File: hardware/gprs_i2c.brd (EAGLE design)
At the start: 50 x 38 mm, 88 parts, among them IC1 SIM900, J2 U.FL, Q1 si2305cd, Q2 PMBF170, Q3 PMBF170, Q4 si2305cd, Q5 si2305cd, T1 BC846, T2 BC846, T3 BC846, T4 BC846, U1 SPX5205 3v3, U3 TC1014 2V8, X2 bat, X3 prog, X4 ts, X5 MOLEX_4HORIZONTAL, X6 MOLEX_4HORIZONTAL, Y1 32768Hz CFPX-217 12.5pF

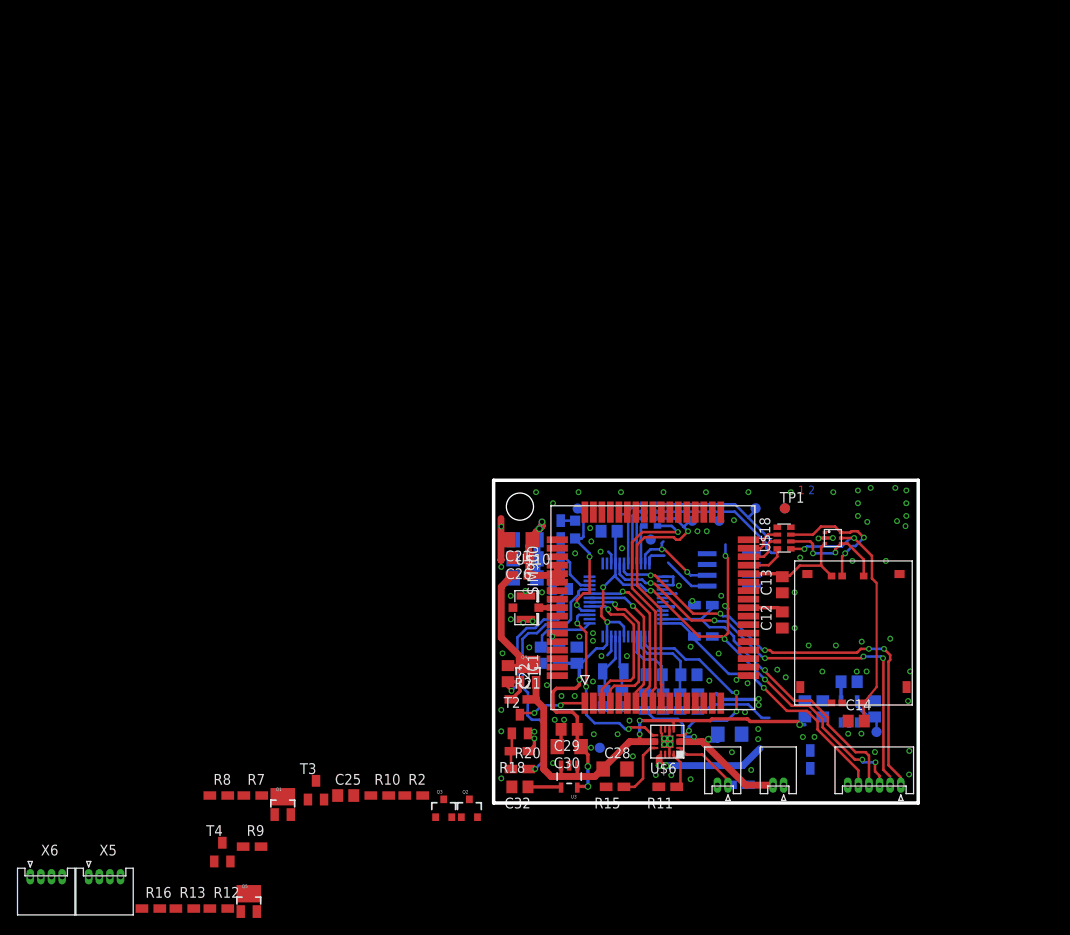
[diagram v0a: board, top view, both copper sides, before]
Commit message: pcb routing stage1
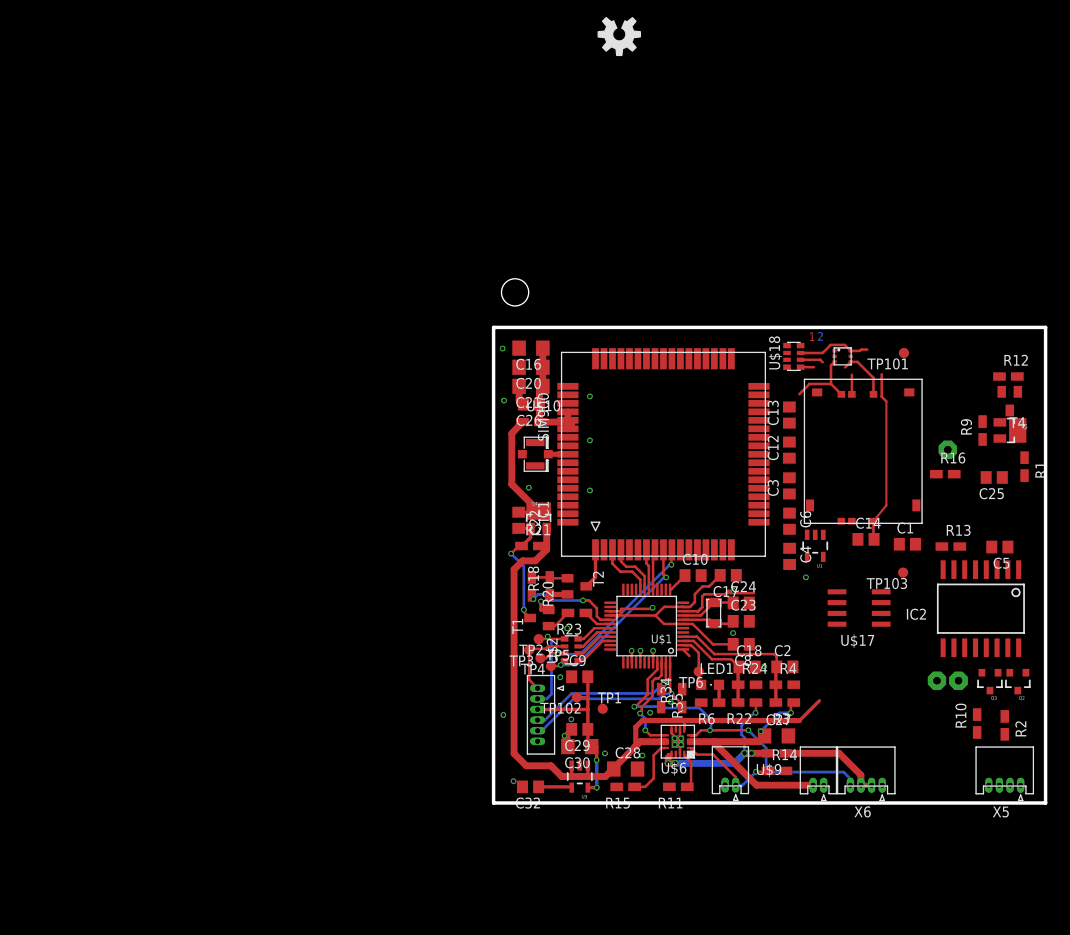
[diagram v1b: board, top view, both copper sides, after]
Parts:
- removed C15: 100uF, rcl:C1206
- removed Q1: si2305cd, Simplex-DiscreteSemi:SOT23-3_POWER@1
- removed R7: 220K, rcl:R0805W
- removed R8: 100K, rcl:R0805W
- removed T3: BC846, transistor:SOT23
- removed X3: prog, Simplex-Connectors:0530480610
- added C5: 100nF, rcl:C0805
- added G1: HU2032-LF, Simplex-Battery:HU2032-LF
- added IC2: DS3231, Simplex-ICs:SO-16
- added R1: 10k, rcl:R0805W
- added X1: prog, Simplex-Connectors:0530470610
- X5: value MOLEX_4HORIZONTAL -> i2c
- X6: value MOLEX_4HORIZONTAL -> pwr
- moved R12 112.1 mm to (60.6, 50.2)
- moved X5 110.3 mm to (62.1, 2.09), turned to 180 degrees
- moved T4 106.8 mm to (60.8, 47.3), turned to 180 degrees
- moved R16 106.6 mm to (53.2, 38.7)
- moved Q5 105.5 mm to (61.0, 43.9), turned to 270 degrees
- moved X6 100.9 mm to (45.8, 2.09), turned to 180 degrees
- moved R13 99.8 mm to (53.8, 30.2)
- moved R9 99.0 mm to (57.6, 43.9), turned to 90 degrees
- moved C25 85.0 mm to (59.0, 38.3), turned to 180 degrees
- moved U$7 84.0 mm to (14.8, 90.5), flipped to the top, turned to 180 degrees
- moved R10 70.9 mm to (56.9, 9.36), turned to 90 degrees
- moved R2 70.1 mm to (60.2, 9.14), turned to 270 degrees
- moved Q2 66.3 mm to (61.7, 14.3), turned to 180 degrees
- moved Q3 66.1 mm to (58.5, 14.3), turned to 180 degrees
- moved TP1 31.9 mm to (12.8, 11.1)
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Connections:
- removed net 46: U$1.46
- removed net N$12: Q1.1, R7.2, T3.3
- removed net N$13: R8.2, T3.1
- removed net P4.0: U$1.29
- removed net P4.1: U$1.30
- new net N$9: IC2.1, R1.2
- net 2V8: now also X1.3; no longer X3.3
- net 2V8_SW: now also C5.1, IC2.2, R1.1
- net CE: now also U$1.45; no longer U$1.2
- net CHG: now also U$1.46; no longer U$1.15
- net CTS: now also U$1.18; no longer U$1.19
- net DTR: now also U$1.20; no longer U$1.17
- net GND: now also C5.2, G1.-, IC2.10, IC2.11, IC2.12, IC2.13, IC2.4, IC2.5, IC2.6, IC2.7, IC2.8, IC2.9, U$17.2, X1.6; no longer C15.2, T3.2, X3.6
- net GPRS_PWRKEY: now also U$1.29; no longer U$1.21
- net GPRS_VBAT: now also U$1.30; no longer U$1.22
- net I2C_EN: now also U1.3; no longer R8.1
- net N$5: now also G1.+, IC2.14; no longer C3.1, C6.1, Q1.3, U1.1, U1.3
- net RI: now also U$1.19; no longer U$1.18
- net RST: now also X1.5; no longer X3.5
- net RTS: now also U$1.17; no longer U$1.20
- net SCL_L: now also IC2.16
- net SDA_L: now also IC2.15
- net STATUS: now also U$1.2; no longer U$1.16
- net TEST: now also X1.4; no longer X3.4
- net UART_RX: now also X1.2; no longer X3.2
- net UART_TX: now also X1.1; no longer X3.1
- net VBAT: no longer C15.1
- net VIN: now also C3.1, C6.1, U1.1; no longer Q1.2, R7.1
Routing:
- net 2V8: track 104.6 -> 48.2 mm, vias 13 -> 2
- net P4.1: track 51.8 -> 0.00 mm, vias 5 -> 0
- net P4.0: track 50.8 -> 0.00 mm, vias 5 -> 0
- net VIN: track 53.6 -> 81.3 mm, vias 3 -> 0
- net GPRS_PWRKEY: track 29.8 -> 11.6 mm, vias 1 -> 2
- net TEST: track 37.5 -> 20.3 mm
- net CE: track 24.4 -> 41.3 mm
- net RTS: track 19.1 -> 4.77 mm, vias 1 -> 0
- net CTS: track 17.9 -> 4.80 mm, vias 1 -> 0
- net RI: track 19.2 -> 6.45 mm, vias 1 -> 0
- net VRAW: track 0.00 -> 12.4 mm
- net DTR: track 18.4 -> 6.86 mm, vias 1 -> 0
- net SIMLOCK_IO: track 32.7 -> 21.8 mm, vias 2 -> 0
- net SCL_L: track 10.9 -> 0.00 mm, vias 2 -> 0
- net CHG: track 22.8 -> 12.1 mm, vias 3 -> 2
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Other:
- board size 50 x 38 mm -> 65 x 56 mm
- board text removed: "10KOhm ts"
- board text removed: "gps"

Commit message: pcb reouting part2
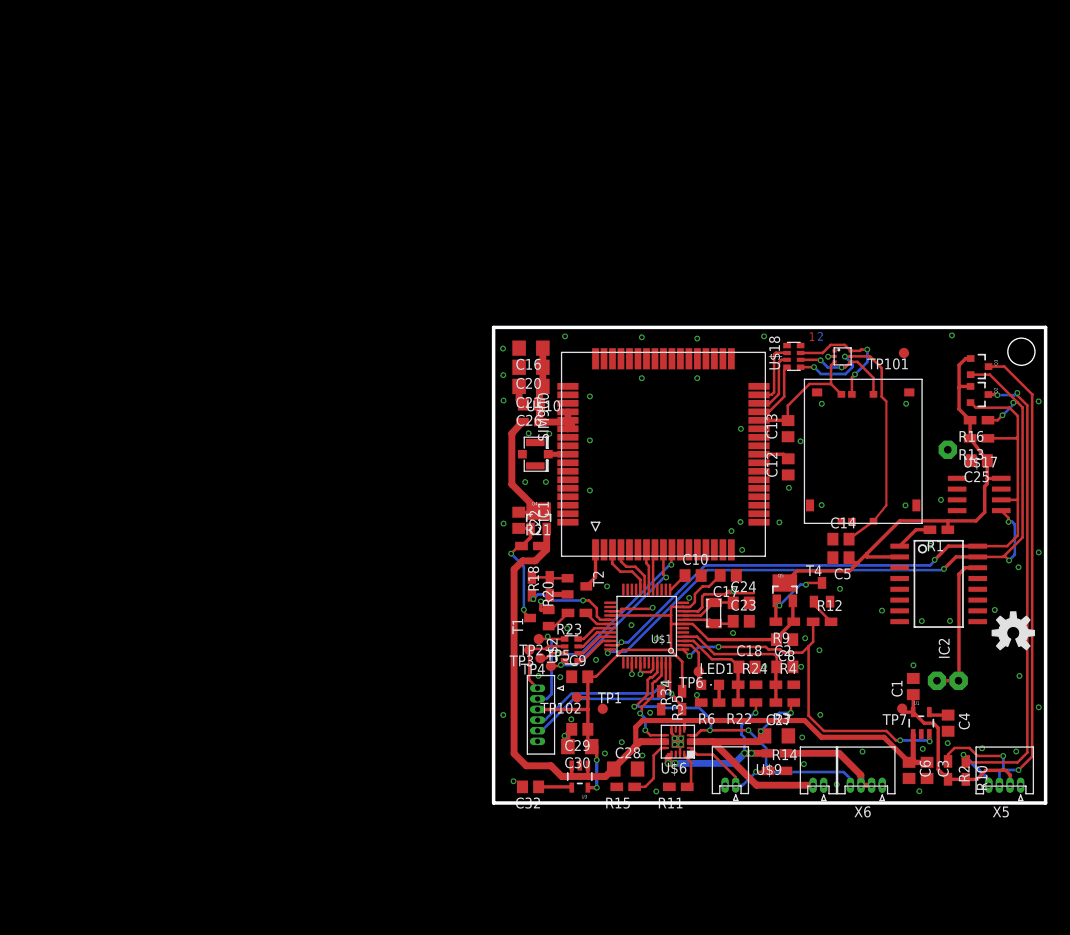
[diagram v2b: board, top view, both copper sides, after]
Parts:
- removed TP103: TPTP12R, testpad:TP12R
- added TP7: TPTP12R, testpad:TP12R
- moved U$7 84.4 mm to (61.2, 20.0), turned to 0 degrees
- moved C3 37.2 mm to (51.0, 3.84), turned to 270 degrees
- moved Q3 37.1 mm to (57.2, 51.4), turned to 270 degrees
- moved R12 36.3 mm to (38.7, 21.3)
- moved Q2 34.1 mm to (57.2, 48.1), turned to 270 degrees
- moved Q5 32.6 mm to (34.3, 25.2), turned to 0 degrees
- moved C6 32.5 mm to (48.9, 3.84)
- moved R9 32.4 mm to (34.3, 21.4), turned to 180 degrees
- moved T4 31.6 mm to (38.7, 24.8), turned to 0 degrees
- moved C4 27.1 mm to (53.5, 9.40)
- moved U1 24.3 mm to (50.4, 9.40), turned to 0 degrees
- moved U$17 19.5 mm to (57.2, 36.3), turned to 270 degrees
- moved C5 18.8 mm to (40.9, 28.9)
- moved C1 16.8 mm to (49.4, 13.7), turned to 90 degrees
- moved R13 13.2 mm to (57.2, 42.9), turned to 180 degrees
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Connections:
- net +3V3: now also TP7.TP; no longer TP103.TP
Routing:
- net SDA_L: track 0.00 -> 90.5 mm, vias 0 -> 6
- net SCL_L: track 0.00 -> 79.2 mm, vias 0 -> 2
- net SDA_H: track 0.00 -> 65.0 mm, vias 0 -> 2
- net SCL_H: track 0.00 -> 59.9 mm, vias 0 -> 3
- net 2V8_SW: track 0.00 -> 57.0 mm
- net I2C_EN: track 1.09 -> 43.8 mm, vias 0 -> 4
- net 2V8: track 48.2 -> 78.2 mm
- net +3V3: track 0.00 -> 23.2 mm
- net N$5: track 0.00 -> 17.7 mm
- net VIN: track 81.3 -> 98.4 mm
- net SIMLOCK_IO: track 21.8 -> 35.7 mm, vias 0 -> 2
- net N$14: track 0.00 -> 9.24 mm, vias 0 -> 2
- net N$19: track 0.00 -> 7.96 mm
- net N$18: track 0.00 -> 7.59 mm
- net N$17: track 0.00 -> 7.31 mm
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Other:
- board text added: "Petre Rodan 201510 rev1"
- board text added: "github.com/rodan/gprs_i2c_gateway"
- board text added: "i2c"
- board text added: "tp7"
- board text added: "tp8"
- board text removed: "+2V8"
- board text removed: "+3V3"
- board text removed: "Petre Rodan 201411 rev2.1"
- board text removed: "github.com/rodan/tracy"

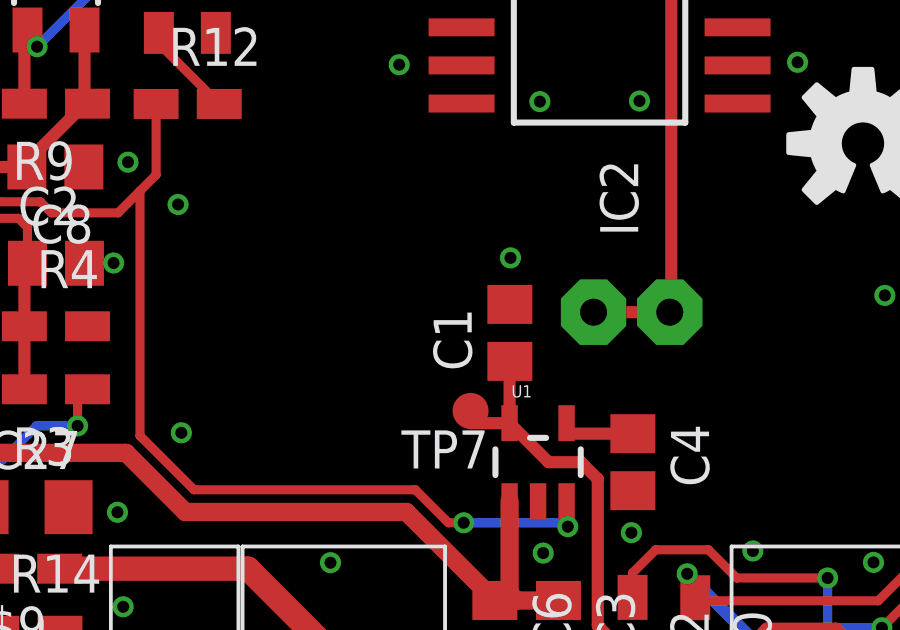
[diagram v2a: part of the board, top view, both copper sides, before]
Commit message: add sensor board
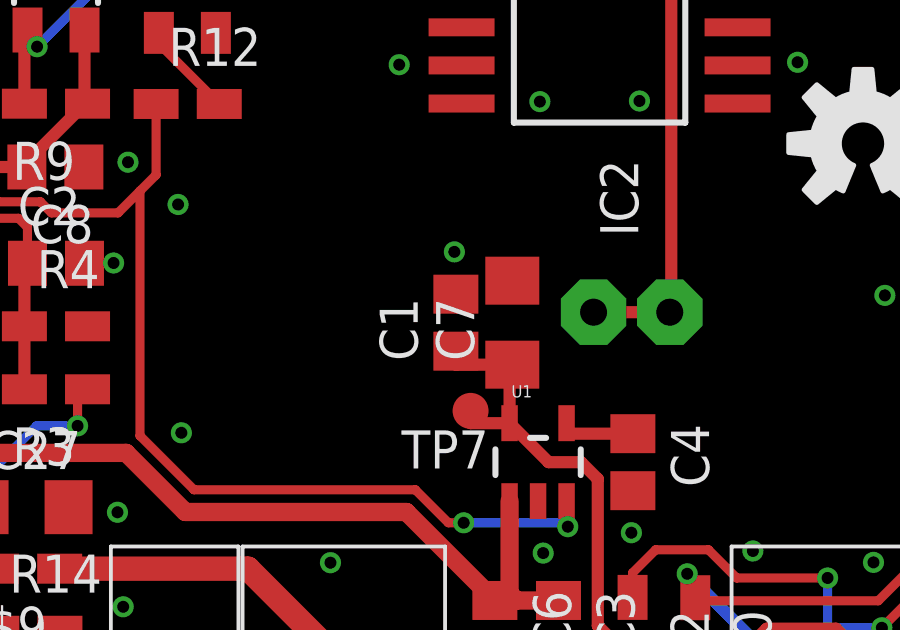
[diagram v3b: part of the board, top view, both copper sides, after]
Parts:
- added C7: 10uF, rcl:C1206
- moved C1 1.83 mm to (47.6, 14.1)
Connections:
- net +3V3: now also C7.1
- net GND: now also C7.2
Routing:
- net +3V3: track 23.2 -> 25.6 mm
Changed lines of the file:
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@@
 <grid distance="0.01" unitdist="mm" unit="mm" style="dots" multiple="1" display="no" altdistance="0.635" altunitdist="mm" altunit="mm"/>
 <layers>
-<layer number="1" name="Top" color="4" fill="1" visible="yes" active="yes"/>
-<layer number="2" name="Route2" color="1" fill="3" visible="yes" active="yes"/>
+<layer number="1" name="Top" color="4" fill="1" visible="no" active="yes"/>
+<layer number="2" name="Route2" color="1" fill="3" visible="no" active="yes"/>
 <layer number="3" name="Route3" color="4" fill="3" visible="no" active="no"/>
 <layer number="14" name="Route14" color="1" fill="6" visible="no" active="no"/>
-<layer number="15" name="Route15" color="4" fill="6" visible="yes" active="yes"/>
-<layer number="16" name="Bottom" color="1" fill="1" visible="yes" active="yes"/>
+<layer number="15" name="Route15" color="4" fill="6" visible="no" active="yes"/>
+<layer number="16" name="Bottom" color="1" fill="1" visible="no" active="yes"/>
 <layer number="17" name="Pads" color="2" fill="1" visible="yes" active="yes"/>
 <layer number="18" name="Vias" color="2" fill="1" visible="yes" active="yes"/>
@@
 <layer number="29" name="tStop" color="7" fill="3" visible="no" active="yes"/>
 <layer number="30" name="bStop" color="7" fill="6" visible="no" active="yes"/>
-<layer number="31" name="tCream" color="7" fill="4" visible="no" active="yes"/>
-<layer number="32" name="bCream" color="7" fill="5" visible="no" active="yes"/>
+<layer number="31" name="tCream" color="7" fill="4" visible="yes" active="yes"/>
+<layer number="32" name="bCream" color="7" fill="5" visible="yes" active="yes"/>
 <layer number="33" name="tFinish" color="6" fill="3" visible="no" active="yes"/>
 <layer number="34" name="bFinish" color="6" fill="6" visible="no" active="yes"/>
@@
 <rectangle x1="17.8" y1="5.1" x2="21.8" y2="9.4" layer="30"/>
 <text x="7.18" y="12.05" size="0.8128" layer="109" font="vector" ratio="15">tp8</text>
-<text x="13.75" y="10.79" size="0.8128" layer="109" font="vector" ratio="15">tp1</text>
+<text x="45.53" y="52.63" size="0.8128" layer="109" font="vector" ratio="15">tp1</text>
 <text x="2.8" y="18.93" size="0.8128" layer="109" font="vector" ratio="15">tp2</text>
 <text x="1.67" y="17.64" size="0.8128" layer="109" font="vector" ratio="15">tp3</text>
@@
 <elements>
 <element name="U1" library="SparkFun" package="SOT23-5" value="SPX5205 3v3" x="50.36" y="9.4"/>
-<element name="C1" library="rcl" package="C0805" value="100nF" x="49.42" y="13.71" rot="R90"/>
+<element name="C1" library="rcl" package="C0805" value="100nF" x="47.62" y="14.05" rot="R90"/>
 <element name="C4" library="rcl" package="C0805" value="1uF" x="53.52" y="9.4" rot="R270"/>
 <element name="C6" library="rcl" package="C0805" value="100nF" x="48.92" y="3.84" rot="R270"/>
@@
 <element name="R1" library="rcl" package="R0805W" value="10k" x="52.43" y="32.18" rot="R180"/>
 <element name="X1" library="Simplex-Connectors" package="0530470610" value="prog" x="5.18" y="13.51" rot="R270"/>
+<element name="C7" library="rcl" package="C1206" value="10uF" x="49.5" y="14.05" rot="R90"/>
 </elements>
 <signals>
@@
 <via x="40.41" y="2.17" extent="1-16" drill="0.4"/>
 <via x="50.13" y="1.39" extent="1-16" drill="0.4"/>
-<via x="49.44" y="16.21" extent="1-16" drill="0.4"/>
+<via x="47.57" y="16.41" extent="1-16" drill="0.4"/>
 <via x="15.09" y="7.16" extent="1-16" drill="0.4"/>
 <via x="5.29" y="14.96" extent="1-16" drill="0.4"/>
 <via x="1.14" y="50.38" extent="1-16" drill="0.4"/>
 <wire x1="24.1" y1="22.57" x2="24.09" y2="22.58" width="0.3048" layer="1"/>
+<contactref element="C7" pad="2"/>
 </signal>
 <signal name="VIN">
@@
 <wire x1="60.82" y1="2.1" x2="60.81" y2="2.09" width="0.4064" layer="1"/>
 <wire x1="49.41" y1="10.7001" x2="49.41" y2="12.76" width="0.4064" layer="1"/>
-<wire x1="49.41" y1="12.76" x2="49.42" y2="12.76" width="0.4064" layer="1"/>
 <wire x1="48.11" y1="11.11" x2="48.11" y2="10.7001" width="0.4064" layer="1"/>
 <wire x1="48.11" y1="10.7001" x2="49.41" y2="10.7001" width="0.4064" layer="1"/>
+<contactref element="C7" pad="1"/>
+<wire x1="49.5" y1="12.65" x2="47.62" y2="12.65" width="0.4064" layer="1"/>
+<wire x1="47.62" y1="12.65" x2="47.62" y2="13.1" width="0.4064" layer="1"/>
+<wire x1="49.41" y1="12.76" x2="49.5" y2="12.65" width="0" layer="19" extent="1-1"/>
 </signal>
 <signal name="N$6">
